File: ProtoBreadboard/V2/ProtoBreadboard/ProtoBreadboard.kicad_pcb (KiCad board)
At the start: 2 copper layers, 180.3 x 162.6 mm, 63 parts, among them IC1 AT90USB1286-AU, IC2 BSS138, IC3 BSS138, J1 Conn_01x30_Female, J10 Conn_01x04_Female, J11 Conn_01x32_Female, J12 Conn_01x06_Female, J13 Conn_01x08_Female, J14 Conn_01x08_Female, J15 Conn_01x04_Female, J16 Conn_01x03_Female, J17 Conn_01x03_Female, J18 Conn_01x07_Female, J19 Conn_01x02_Female, J2 Conn_01x10_Female, J20 Conn_01x02_Female, J21 Conn_01x02_Female, J22 AVR-ISP-6, J23 Conn_01x02_Female, J24 Conn_01x03_Female, J25 Conn_01x07_Female, J26 Conn_01x03_Female, J27 Conn_02x03_Counter_Clockwise, J28 Conn_01x03_Female, J29 Conn_01x02_Female, J3 Conn_01x32_Female, J30 Conn_01x02_Female, J31 Conn_01x02_Female, J32 Conn_01x02_Female, J4 Conn_01x10_Female, J5 Conn_01x30_Female, J6 Conn_01x02_Female, J7 Conn_01x02_Female, J8 Conn_01x06_Female, J9 Conn_01x04_Female, SW1 RotaryEncoder_Switch, SW2 RotaryEncoder_Switch, U1 IS31FL3741A, U2 AP2112K-3.3, U3 PRTR5V0U2X, Y1 Crystal

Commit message: Completed V2 Breadboard
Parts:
- moved J11 89.2 mm to (132.1, 180.3), turned to 180 degrees
- moved J3 79.7 mm to (101.6, 101.6), turned to 0 degrees
- moved IC1 7.62 mm to (116.8, 142.2), turned to -45 degrees
- moved J26 4.53 mm to (21.5, 68.6)
- moved J27 4.53 mm to (26.6, 68.6)
- moved U2 4.53 mm to (27.8, 83.9)
- moved J20 4.53 mm to (34.2, 83.8)
- moved J28 4.53 mm to (34.2, 68.6)
- moved J17 4.53 mm to (21.5, 53.3)
- moved J22 4.53 mm to (26.6, 53.3)
- moved J16 4.53 mm to (21.5, 81.3)
- moved J24 4.53 mm to (34.2, 53.3)
- moved IC2 2.27 mm to (25.1, 99.1)
- moved IC3 2.27 mm to (27.7, 104.2)
- moved J15 2.27 mm to (20.0, 96.5)
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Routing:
- net Net-(G9-Pad2): track 4.80 -> 0.00 mm
- net Net-(G8-Pad2): track 4.80 -> 9.60 mm
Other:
- board size 180.3 x 162.6 mm -> 179 x 167.6 mm
- board text added: "12G"
- board text added: "1G"
- board text added: "22G"
- board text added: "2G"
- board text added: "30G"
- board text added: "36G"
- board text added: "53G"
- board text added: "55G"
- board text added: "61"
- board text added: "62"
- board text added: "63G"
- board text added: "64"
- board text added: "6G"
- board text removed: "GND"

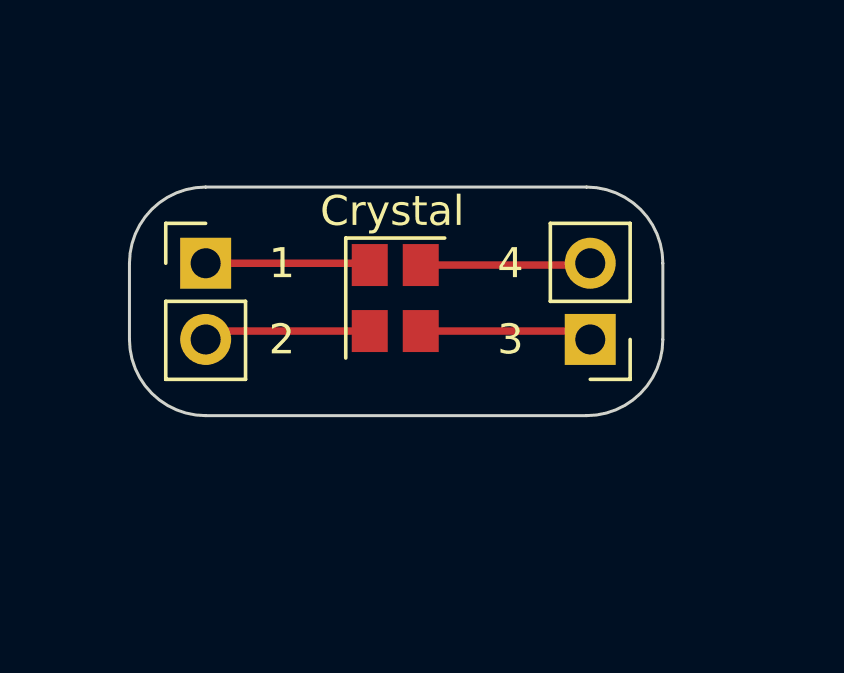
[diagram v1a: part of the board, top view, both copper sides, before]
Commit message: Fixing small crystal 2.54mm layout problem
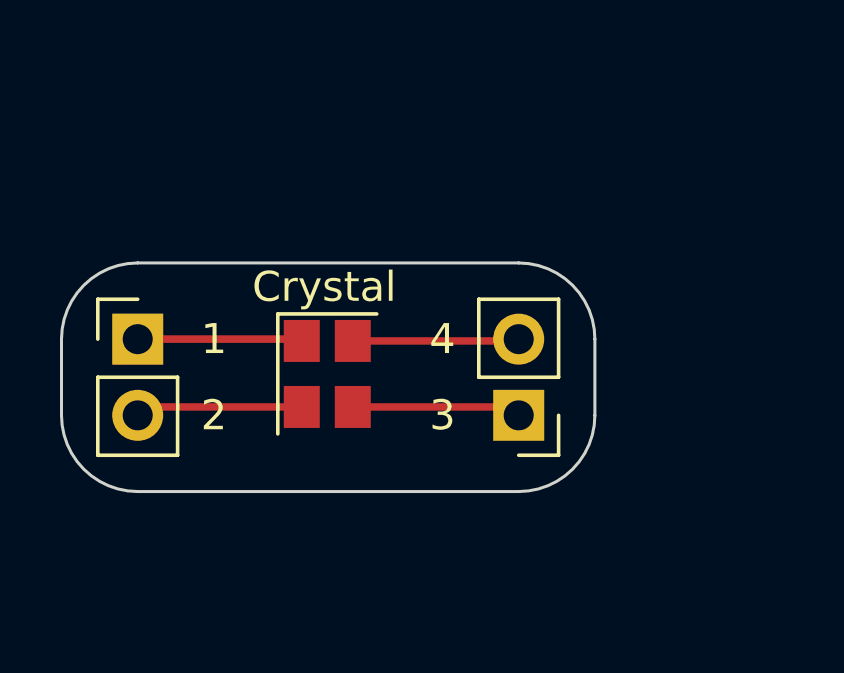
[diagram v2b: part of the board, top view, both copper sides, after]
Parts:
- moved J7 3.48 mm to (30.5, 134.6)
- moved J6 3.40 mm to (17.8, 132.1)
- moved Y1 3.40 mm to (24.1, 133.2)
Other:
- board size 179 x 167.6 mm -> 180.3 x 167.6 mm
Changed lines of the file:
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@@
   )
   (footprint "Connector_PinHeader_2.54mm:PinHeader_1x02_P2.54mm_Vertical" (layer "F.Cu")
-    (at 20.045 129.55)
+    (at 17.78 132.08)
     (descr "Through hole straight pin header, 1x02, 2.54mm pitch, single row")
     (tags "Through hole pin header THT 1x02 2.54mm single row")
@@
   )
   (footprint "Crystal:Crystal_SMD_3225-4Pin_3.2x2.5mm" (layer "F.Cu")
-    (at 26.365 130.71 -90)
+    (at 24.1 133.24 -90)
     (descr "SMD Crystal SERIES SMD3225/4 http://www.txccrystal.com/images/pdf/7m-accuracy.pdf, 3.2x2.5mm^2 package")
     (tags "SMD SMT crystal")
@@
   )
   (footprint "Connector_PinHeader_2.54mm:PinHeader_1x02_P2.54mm_Vertical" (layer "F.Cu")
-    (at 32.865 132.09 180)
+    (at 30.48 134.62 180)
     (descr "Through hole straight pin header, 1x02, 2.54mm pitch, single row")
     (tags "Through hole pin header THT 1x02 2.54mm single row")
@@
   (gr_line (start 71.120001 43.180001) (end 71.12 17.779999) (layer "Edge.Cuts") (width 0.1))
   (gr_line (start 43.18 50.8) (end 43.18 127) (layer "Edge.Cuts") (width 0.1))
-  (gr_line (start 35.285 132.09) (end 35.285 129.55) (layer "Edge.Cuts") (width 0.1))
-  (gr_arc (start 20.045 134.63) (mid 18.248949 133.886051) (end 17.505 132.09) (layer "Edge.Cuts") (width 0.1))
+  (gr_line (start 33.02 134.62) (end 33.02 132.08) (layer "Edge.Cuts") (width 0.1))
+  (gr_arc (start 17.78 137.16) (mid 15.983949 136.416051) (end 15.24 134.62) (layer "Edge.Cuts") (width 0.1))
   (gr_line (start 36.769999 73.66) (end 36.769999 68.58) (layer "Edge.Cuts") (width 0.1))
   (gr_line (start 127 15.24) (end 109.22 15.24) (layer "Edge.Cuts") (width 0.1))
@@
   (gr_arc (start 78.5525 38.225) (mid 76.756449 37.481051) (end 76.0125 35.685) (layer "Edge.Cuts") (width 0.1))
   (gr_line (start 32.745001 111.769999) (end 20.045 111.77) (layer "Edge.Cuts") (width 0.1))
-  (gr_line (start 32.745 127.01) (end 20.045 127.01) (layer "Edge.Cuts") (width 0.1))
+  (gr_line (start 30.48 129.54) (end 17.78 129.54) (layer "Edge.Cuts") (width 0.1))
   (gr_line (start 98.8725 35.685) (end 98.8725 17.905) (layer "Edge.Cuts") (width 0.1))
-  (gr_arc (start 17.505 129.55) (mid 18.248949 127.753949) (end 20.045 127.01) (layer "Edge.Cuts") (width 0.1))
-  (gr_line (start 20.045 134.63) (end 32.745 134.63) (layer "Edge.Cuts") (width 0.1))
+  (gr_arc (start 15.24 132.08) (mid 15.983949 130.283949) (end 17.78 129.54) (layer "Edge.Cuts") (width 0.1))
+  (gr_line (start 17.78 137.16) (end 30.48 137.16) (layer "Edge.Cuts") (width 0.1))
   (gr_line (start 34.229999 66.04) (end 21.529999 66.04) (layer "Edge.Cuts") (width 0.1))
   (gr_arc (start 18.99 53.34) (mid 19.733949 51.543949) (end 21.53 50.8) (layer "Edge.Cuts") (width 0.1))
@@
   (gr_arc (start 170.18 22.86) (mid 170.923949 21.063949) (end 172.72 20.32) (layer "Edge.Cuts") (width 0.1))
   (gr_arc (start 17.505 96.53) (mid 18.248949 94.733949) (end 20.045 93.99) (layer "Edge.Cuts") (width 0.1))
-  (gr_arc (start 32.745 127.01) (mid 34.541051 127.753949) (end 35.285 129.55) (layer "Edge.Cuts") (width 0.1))
+  (gr_arc (start 30.48 129.54) (mid 32.276051 130.283949) (end 33.02 132.08) (layer "Edge.Cuts") (width 0.1))
   (gr_arc (start 132.08 99.06) (mid 133.876051 99.803949) (end 134.62 101.6) (layer "Edge.Cuts") (width 0.1))
   (gr_line (start 101.6 99.06) (end 132.08 99.06) (layer "Edge.Cuts") (width 0.1))
@@
   (gr_line (start 170.18 22.86) (end 170.18 96.52) (layer "Edge.Cuts") (width 0.1))
   (gr_line (start 134.62 86.36) (end 134.62 50.8) (layer "Edge.Cuts") (width 0.1))
-  (gr_line (start 17.505 129.55) (end 17.505 132.09) (layer "Edge.Cuts") (width 0.1))
+  (gr_line (start 15.24 132.08) (end 15.24 134.62) (layer "Edge.Cuts") (width 0.1))
   (gr_line (start 16.59345 18.38) (end 16.59345 41.24) (layer "Edge.Cuts") (width 0.1))
   (gr_line (start 96.3325 15.365) (end 78.5525 15.365) (layer "Edge.Cuts") (width 0.1))
   (gr_arc (start 21.529999 76.200001) (mid 19.733948 75.456052) (end 18.989999 73.660001) (layer "Edge.Cuts") (width 0.1))
-  (gr_arc (start 35.285 132.09) (mid 34.541051 133.886051) (end 32.745 134.63) (layer "Edge.Cuts") (width 0.1))
+  (gr_arc (start 33.02 134.62) (mid 32.276051 136.416051) (end 30.48 137.16) (layer "Edge.Cuts") (width 0.1))
   (gr_line (start 31.833451 15.839999) (end 19.13345 15.84) (layer "Edge.Cuts") (width 0.1))
   (gr_arc (start 43.18 17.78) (mid 43.923949 15.983949) (end 45.72 15.24) (layer "Edge.Cuts") (width 0.1))
@@
     (effects (font (size 1 1) (thickness 0.15)))
   )
-  (gr_text "2" (at 22.585 132.09) (layer "F.SilkS")
+  (gr_text "2" (at 20.32 134.62) (layer "F.SilkS")
     (effects (font (size 1 1) (thickness 0.15)))
   )
@@
     (effects (font (size 1 1) (thickness 0.15)))
   )
-  (gr_text "4" (at 30.205 129.55) (layer "F.SilkS")
+  (gr_text "4" (at 27.94 132.08) (layer "F.SilkS")
     (effects (font (size 1 1) (thickness 0.15)))
   )
@@
     (effects (font (size 1 1) (thickness 0.15)))
   )
-  (gr_text "3" (at 30.205 132.09) (layer "F.SilkS")
+  (gr_text "3" (at 27.94 134.62) (layer "F.SilkS")
     (effects (font (size 1 1) (thickness 0.15)))
   )
@@
     (effects (font (size 1 1) (thickness 0.15)))
   )
-  (gr_text "1" (at 22.585 129.55) (layer "F.SilkS")
+  (gr_text "1" (at 20.32 132.08) (layer "F.SilkS")
     (effects (font (size 1 1) (thickness 0.15)))
   )
@@
   )
   (dimension (type aligned) (layer "Cmts.User")
-    (pts (xy 20.045 127.01) (xy 20.045 134.63))
+    (pts (xy 17.78 129.54) (xy 17.78 137.16))
     (height 4.805)
-    (gr_text "7.6200 mm" (at 14.09 130.82 90) (layer "Cmts.User")
+    (gr_text "7.6200 mm" (at 11.825 133.35 90) (layer "Cmts.User")
       (effects (font (size 1 1) (thickness 0.15)))
     )
@@
   )
   (dimension (type aligned) (layer "Cmts.User")
-    (pts (xy 17.505 132.09) (xy 35.285 132.09))
+    (pts (xy 15.24 134.62) (xy 33.02 134.62))
     (height 5.07)
-    (gr_text "17.7800 mm" (at 26.395 136.01) (layer "Cmts.User")
+    (gr_text "17.7800 mm" (at 24.13 138.54) (layer "Cmts.User")
       (effects (font (size 1 1) (thickness 0.15)))
     )
@@
   (segment (start 193.04 73.66) (end 188.88564 69.50564) (width 0.2) (layer "F.Cu") (net 108))
   (segment (start 188.88564 65.834269) (end 185.885204 62.833833) (width 0.2) (layer "F.Cu") (net 108))
-  (segment (start 25.455 129.55) (end 25.515 129.61) (width 0.25) (layer "F.Cu") (net 109))
-  (segment (start 20.045 129.55) (end 25.455 129.55) (width 0.25) (layer "F.Cu") (net 109))
-  (segment (start 25.515 131.81) (end 20.325 131.81) (width 0.25) (layer "F.Cu") (net 110))
-  (segment (start 20.325 131.81) (end 20.045 132.09) (width 0.25) (layer "F.Cu") (net 110))
-  (segment (start 32.585 131.81) (end 32.865 132.09) (width 0.25) (layer "F.Cu") (net 111))
-  (segment (start 27.215 131.81) (end 32.585 131.81) (width 0.25) (layer "F.Cu") (net 111))
-  (segment (start 32.805 129.61) (end 32.865 129.55) (width 0.25) (layer "F.Cu") (net 112))
-  (segment (start 27.215 129.61) (end 32.805 129.61) (width 0.25) (layer "F.Cu") (net 112))
+  (segment (start 23.19 132.08) (end 23.25 132.14) (width 0.25) (layer "F.Cu") (net 109))
+  (segment (start 17.78 132.08) (end 23.19 132.08) (width 0.25) (layer "F.Cu") (net 109))
+  (segment (start 23.25 134.34) (end 18.06 134.34) (width 0.25) (layer "F.Cu") (net 110))
+  (segment (start 18.06 134.34) (end 17.78 134.62) (width 0.25) (layer "F.Cu") (net 110))
+  (segment (start 30.32 134.34) (end 30.6 134.62) (width 0.25) (layer "F.Cu") (net 111))
+  (segment (start 24.95 134.34) (end 30.32 134.34) (width 0.25) (layer "F.Cu") (net 111))
+  (segment (start 30.54 132.14) (end 30.6 132.08) (width 0.25) (layer "F.Cu") (net 112))
+  (segment (start 24.95 132.14) (end 30.54 132.14) (width 0.25) (layer "F.Cu") (net 112))
   (segment (start 45.72 25.4) (end 45.72 25) (width 0.25) (layer "F.Cu") (net 113))
   (segment (start 45.72 25) (end 50.02 20.7) (width 0.25) (layer "F.Cu") (net 113))
